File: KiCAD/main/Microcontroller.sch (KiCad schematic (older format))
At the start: 9 parts

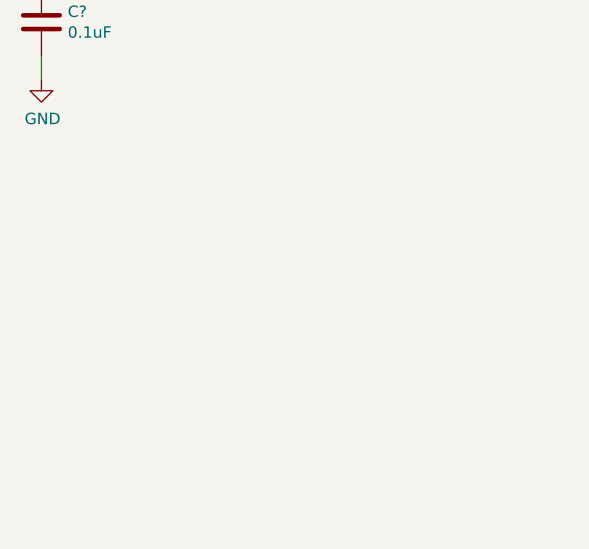
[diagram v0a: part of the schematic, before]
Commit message: Add programming header for the microcontroller
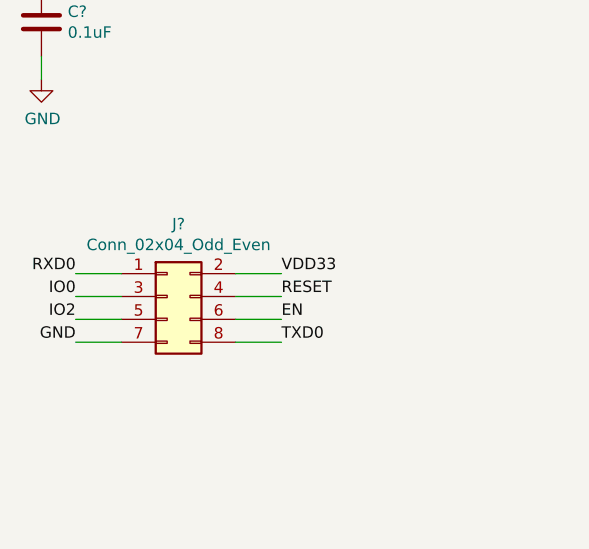
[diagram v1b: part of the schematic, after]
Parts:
- added J?: Conn_02x04_Odd_Even, symbol Connector_Generic:Conn_02x04_Odd_Even
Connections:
- net +3V3: now also J?.2 (Pin_2)
- net EN: now also J?.6 (Pin_6)
- net GND: now also J?.7 (Pin_7)
- net IO0: now also J?.3 (Pin_3)
- net IO2: now also J?.5 (Pin_5)
- net RXD0: now also J?.1 (Pin_1)
- net TXD0: now also J?.8 (Pin_8)
- new net RESET: J?.4 (Pin_4)
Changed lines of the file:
@@
 Text Label 9350 2600 0    50   ~ 0
 TXD0
+$Comp
+L Connector_Generic:Conn_02x04_Odd_Even J?
+U 1 1 5FC4BA04
+P 1650 4500
+F 0 "J?" H 1700 4817 50  0000 C CNN
+F 1 "Conn_02x04_Odd_Even" H 1700 4726 50  0000 C CNN
+F 2 "" H 1650 4500 50  0001 C CNN
+F 3 "~" H 1650 4500 50  0001 C CNN
+	1    1650 4500
+	1    0    0    -1
+$EndComp
+Text Label 1250 4500 2    50   ~ 0
+IO0
+Wire Wire Line
+	1250 4400 1450 4400
+Wire Wire Line
+	1950 4400 2150 4400
+Wire Wire Line
+	1950 4500 2150 4500
+Wire Wire Line
+	1950 4600 2150 4600
+Wire Wire Line
+	1950 4700 2150 4700
+Wire Wire Line
+	1450 4500 1250 4500
+Wire Wire Line
+	1450 4600 1250 4600
+Wire Wire Line
+	1450 4700 1250 4700
+Text Label 1250 4400 2    50   ~ 0
+RXD0
+Text Label 1250 4600 2    50   ~ 0
+IO2
+Text Label 1250 4700 2    50   ~ 0
+GND
+Text Label 2150 4400 0    50   ~ 0
+VDD33
+Text Label 2150 4500 0    50   ~ 0
+RESET
+Text Label 2150 4600 0    50   ~ 0
+EN
+Text Label 2150 4700 0    50   ~ 0
+TXD0
 $EndSCHEMATC

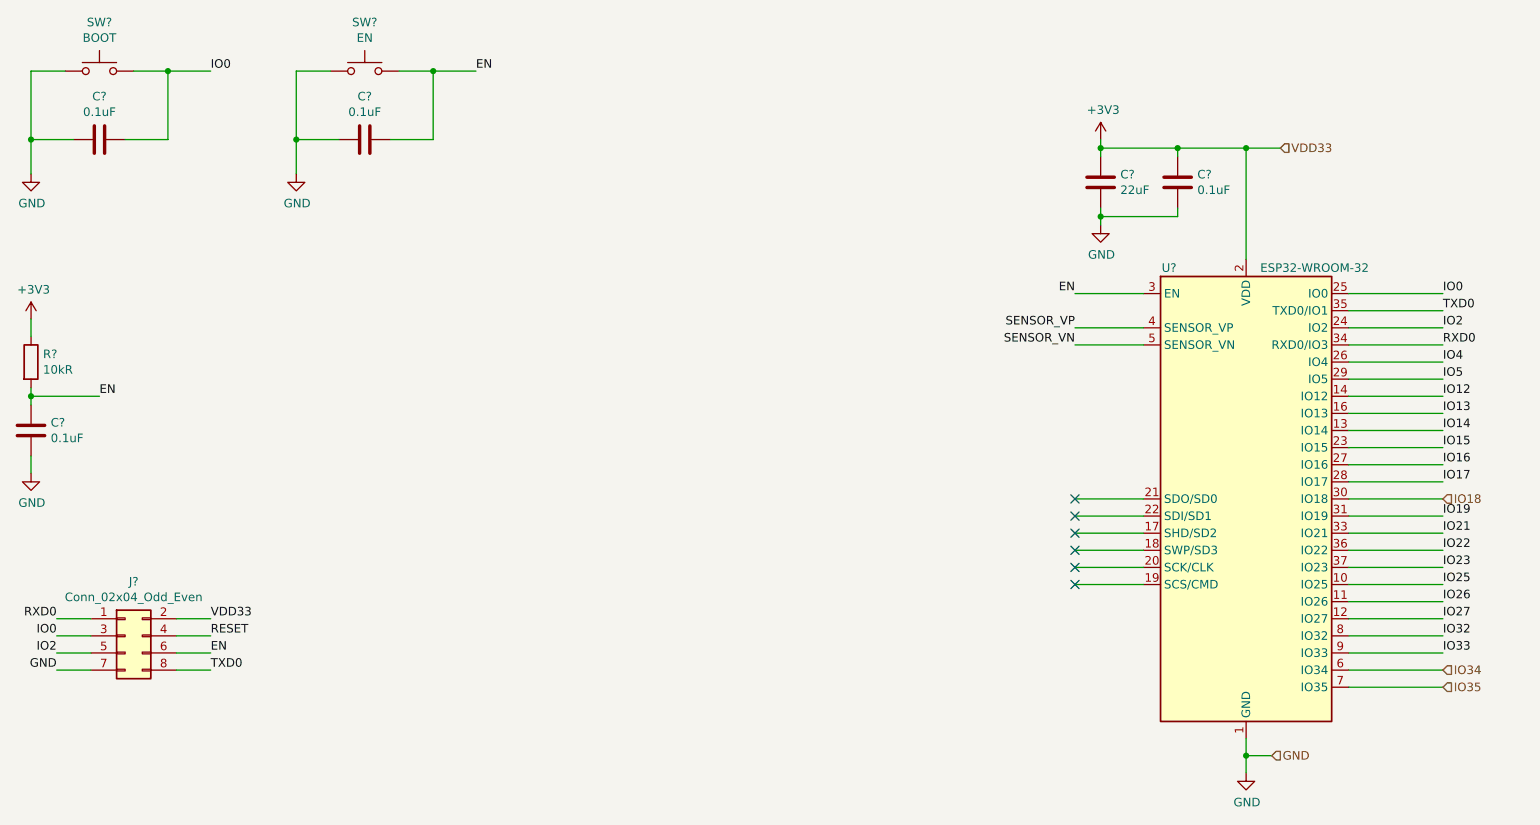
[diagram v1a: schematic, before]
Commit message: Rename EN button to RESET
and add comment about the ENABLE and RESET signals from the programming header
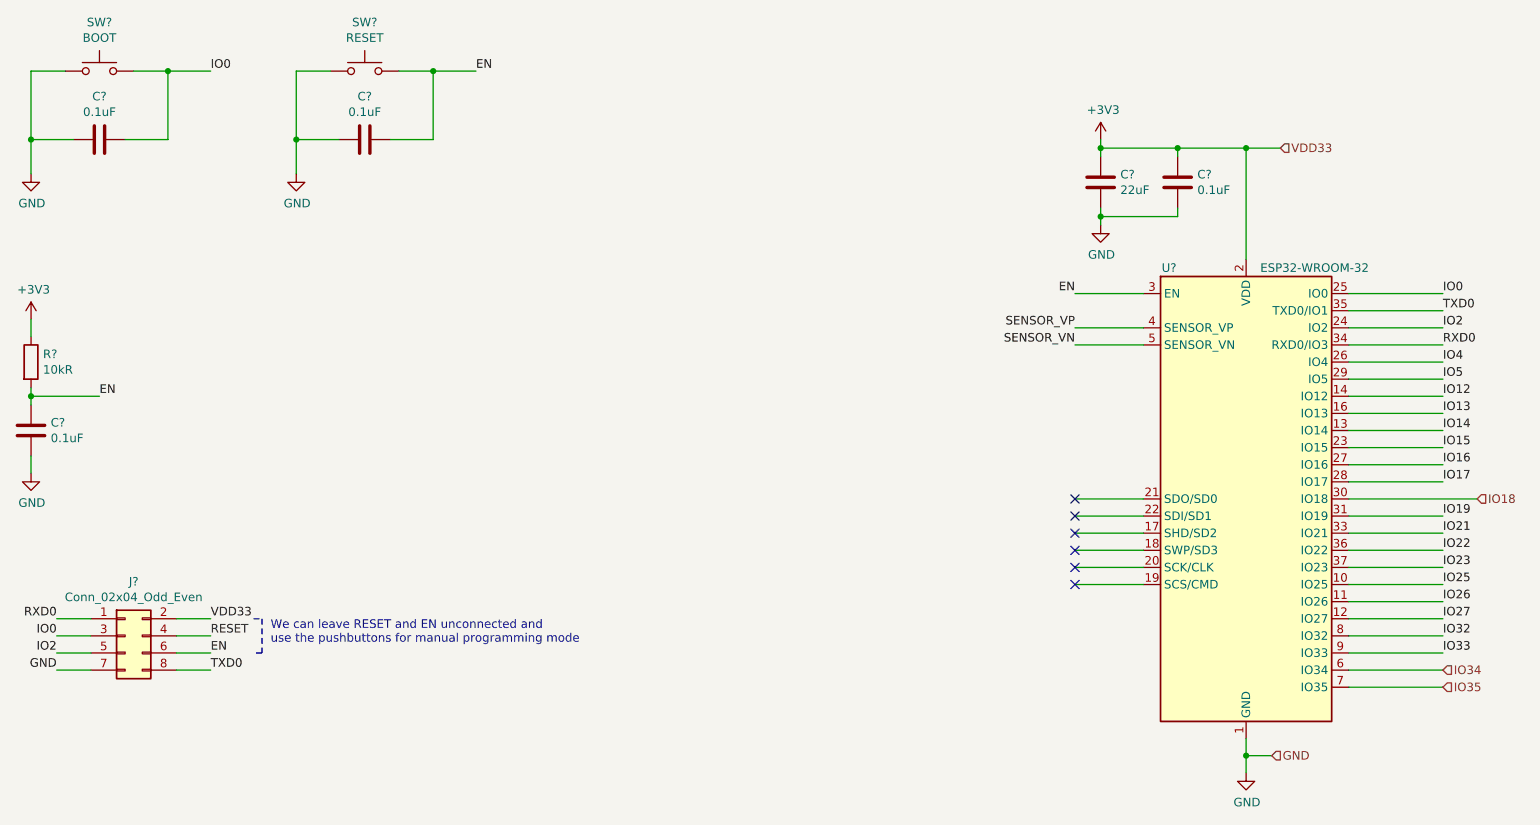
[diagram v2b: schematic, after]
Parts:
- SW?: value EN -> RESET
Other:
- note added: "We can leave RESET and EN unconnected and\nuse the pushbuttons for manual programming mode"
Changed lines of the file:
@@
 P 3050 1200
 F 0 "SW?" H 3050 1485 50  0000 C CNN
-F 1 "EN" H 3050 1394 50  0000 C CNN
+F 1 "RESET" H 3050 1394 50  0000 C CNN
 F 2 "" H 3050 1400 50  0001 C CNN
 F 3 "~" H 3050 1400 50  0001 C CNN
@@
 	8800 3600 9350 3600
 Wire Wire Line
-	8800 3700 9350 3700
-Wire Wire Line
 	8800 3800 9350 3800
 Wire Wire Line
@@
 Wire Wire Line
 	8800 4800 9350 4800
-Text HLabel 9350 3700 2    50   Input ~ 0
+Text HLabel 9550 3700 2    50   Input ~ 0
 IO18
 Text HLabel 9350 4700 2    50   Input ~ 0
@@
 Text Label 2150 4700 0    50   ~ 0
 TXD0
+Text Notes 2500 4550 0    50   ~ 0
+We can leave RESET and EN unconnected and\nuse the pushbuttons for manual programming mode
+Wire Notes Line
+	2400 4400 2450 4400
+Wire Notes Line
+	2450 4400 2450 4600
+Wire Notes Line
+	2450 4600 2400 4600
+Wire Wire Line
+	8800 3700 9550 3700
 $EndSCHEMATC

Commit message: Assign footprints to components on the microcontroller sheet
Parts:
- C? (x5): footprint (none) -> Capacitor_SMD:C_1206_3216Metric
- J?: footprint (none) -> Connector_PinHeader_2.54mm:PinHeader_2x04_P2.54mm_Vertical
- SW? (x2): footprint (none) -> Button_Switch_SMD:SW_SPST_B3S-1000
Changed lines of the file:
@@
 F 0 "C?" H 1215 3346 50  0000 L CNN
 F 1 "0.1uF" H 1215 3255 50  0000 L CNN
-F 2 "" H 1138 3150 50  0001 C CNN
+F 2 "Capacitor_SMD:C_1206_3216Metric" H 1138 3150 50  0001 C CNN
 F 3 "~" H 1100 3300 50  0001 C CNN
 F 4 "50V" H 1215 3255 50  0001 L CNN "Voltage"
@@
 F 0 "C?" H 7915 1896 50  0000 L CNN
 F 1 "0.1uF" H 7915 1805 50  0000 L CNN
-F 2 "" H 7838 1700 50  0001 C CNN
+F 2 "Capacitor_SMD:C_1206_3216Metric" H 7838 1700 50  0001 C CNN
 F 3 "~" H 7800 1850 50  0001 C CNN
 F 4 "50V" H 7915 1759 50  0001 L CNN "Voltage"
@@
 F 0 "C?" H 7465 1896 50  0000 L CNN
 F 1 "22uF" H 7465 1805 50  0000 L CNN
-F 2 "" H 7388 1700 50  0001 C CNN
+F 2 "Capacitor_SMD:C_1206_3216Metric" H 7388 1700 50  0001 C CNN
 F 3 "~" H 7350 1850 50  0001 C CNN
 F 4 "10V" H 7465 1759 50  0001 L CNN "Voltage"
@@
 F 0 "C?" V 1752 1600 50  0000 C CNN
 F 1 "0.1uF" V 1661 1600 50  0000 C CNN
-F 2 "" H 1538 1450 50  0001 C CNN
+F 2 "Capacitor_SMD:C_1206_3216Metric" H 1538 1450 50  0001 C CNN
 F 3 "~" H 1500 1600 50  0001 C CNN
 F 4 "50V" V 1500 1600 50  0001 C CNN "Voltage"
@@
 F 0 "SW?" H 1500 1485 50  0000 C CNN
 F 1 "BOOT" H 1500 1394 50  0000 C CNN
-F 2 "" H 1500 1400 50  0001 C CNN
+F 2 "Button_Switch_SMD:SW_SPST_B3S-1000" H 1500 1400 50  0001 C CNN
 F 3 "~" H 1500 1400 50  0001 C CNN
 	1    1500 1200
@@
 F 0 "C?" V 3302 1600 50  0000 C CNN
 F 1 "0.1uF" V 3211 1600 50  0000 C CNN
-F 2 "" H 3088 1450 50  0001 C CNN
+F 2 "Capacitor_SMD:C_1206_3216Metric" H 3088 1450 50  0001 C CNN
 F 3 "~" H 3050 1600 50  0001 C CNN
 F 4 "50V" V 3050 1600 50  0001 C CNN "Voltage"
@@
 F 0 "SW?" H 3050 1485 50  0000 C CNN
 F 1 "RESET" H 3050 1394 50  0000 C CNN
-F 2 "" H 3050 1400 50  0001 C CNN
+F 2 "Button_Switch_SMD:SW_SPST_B3S-1000" H 3050 1400 50  0001 C CNN
 F 3 "~" H 3050 1400 50  0001 C CNN
 	1    3050 1200
@@
 F 0 "J?" H 1700 4817 50  0000 C CNN
 F 1 "Conn_02x04_Odd_Even" H 1700 4726 50  0000 C CNN
-F 2 "" H 1650 4500 50  0001 C CNN
+F 2 "Connector_PinHeader_2.54mm:PinHeader_2x04_P2.54mm_Vertical" H 1650 4500 50  0001 C CNN
 F 3 "~" H 1650 4500 50  0001 C CNN
 	1    1650 4500

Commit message: Add simple pcb design
still buggy
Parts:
- R2: renamed from R?; footprint (none) -> Resistor_SMD:R_1206_3216Metric
- SW1, SW2: renamed from SW?; footprint Button_Switch_SMD:SW_SPST_B3S-1000 -> Button_Switch_SMD:SW_SPST_PTS645
- gave numbers to parts that had none: 7
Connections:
- net EN: no longer J5.6 (Pin_6)
- net RESET: no longer names the net of J5.4 (Pin_4)
- no-connect marks 6 -> 8
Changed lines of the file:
@@
 $Descr A4 11693 8268
 encoding utf-8
-Sheet 6 6
+Sheet 2 2
 Title "ESP32-DevKitC-V4"
 Date "2020-10-23"
@@
 $EndDescr
 $Comp
-L RF_Module:ESP32-WROOM-32 U?
+L RF_Module:ESP32-WROOM-32 U1
 U 1 1 5F93B762
 P 8200 3700
-F 0 "U?" H 7750 5050 50  0000 C CNN
+F 0 "U1" H 7750 5050 50  0000 C CNN
 F 1 "ESP32-WROOM-32" H 8600 5050 50  0000 C CNN
 F 2 "RF_Module:ESP32-WROOM-32" H 8200 2200 50  0001 C CNN
@@
 $EndComp
 $Comp
-L power:+3V3 #PWR?
+L power:+3V3 #PWR03
 U 1 1 5F9419AA
 P 1100 2650
-F 0 "#PWR?" H 1100 2500 50  0001 C CNN
+F 0 "#PWR03" H 1100 2500 50  0001 C CNN
 F 1 "+3V3" H 1115 2823 50  0000 C CNN
 F 2 "" H 1100 2650 50  0001 C CNN
@@
 $EndComp
 $Comp
-L Device:R R?
+L Device:R R2
 U 1 1 5F94208F
 P 1100 2900
-F 0 "R?" H 1170 2946 50  0000 L CNN
+F 0 "R2" H 1170 2946 50  0000 L CNN
 F 1 "10kR" H 1170 2855 50  0000 L CNN
-F 2 "" V 1030 2900 50  0001 C CNN
+F 2 "Resistor_SMD:R_1206_3216Metric" V 1030 2900 50  0001 C CNN
 F 3 "~" H 1100 2900 50  0001 C CNN
 	1    1100 2900
@@
 $EndComp
 $Comp
-L Device:C C?
+L Device:C C1
 U 1 1 5F9429EB
 P 1100 3300
-F 0 "C?" H 1215 3346 50  0000 L CNN
+F 0 "C1" H 1215 3346 50  0000 L CNN
 F 1 "0.1uF" H 1215 3255 50  0000 L CNN
 F 2 "Capacitor_SMD:C_1206_3216Metric" H 1138 3150 50  0001 C CNN
@@
 $EndComp
 $Comp
-L power:GND #PWR?
+L power:GND #PWR04
 U 1 1 5F942C61
 P 1100 3550
-F 0 "#PWR?" H 1100 3300 50  0001 C CNN
+F 0 "#PWR04" H 1100 3300 50  0001 C CNN
 F 1 "GND" H 1105 3377 50  0000 C CNN
 F 2 "" H 1100 3550 50  0001 C CNN
@@
 	1100 2750 1100 2650
 $Comp
-L power:+3V3 #PWR?
+L power:+3V3 #PWR06
 U 1 1 5F943FB0
 P 7350 1600
-F 0 "#PWR?" H 7350 1450 50  0001 C CNN
+F 0 "#PWR06" H 7350 1450 50  0001 C CNN
 F 1 "+3V3" H 7365 1773 50  0000 C CNN
 F 2 "" H 7350 1600 50  0001 C CNN
@@
 $EndComp
 $Comp
-L Device:C C?
+L Device:C C5
 U 1 1 5F9451F0
 P 7800 1850
-F 0 "C?" H 7915 1896 50  0000 L CNN
+F 0 "C5" H 7915 1896 50  0000 L CNN
 F 1 "0.1uF" H 7915 1805 50  0000 L CNN
 F 2 "Capacitor_SMD:C_1206_3216Metric" H 7838 1700 50  0001 C CNN
@@
 $EndComp
 $Comp
-L Device:C C?
+L Device:C C4
 U 1 1 5F946123
 P 7350 1850
-F 0 "C?" H 7465 1896 50  0000 L CNN
+F 0 "C4" H 7465 1896 50  0000 L CNN
 F 1 "22uF" H 7465 1805 50  0000 L CNN
 F 2 "Capacitor_SMD:C_1206_3216Metric" H 7388 1700 50  0001 C CNN
@@
 	7350 2050 7350 2000
 $Comp
-L power:GND #PWR?
+L power:GND #PWR07
 U 1 1 5F947B11
 P 7350 2100
-F 0 "#PWR?" H 7350 1850 50  0001 C CNN
+F 0 "#PWR07" H 7350 1850 50  0001 C CNN
 F 1 "GND" H 7355 1927 50  0000 C CNN
 F 2 "" H 7350 2100 50  0001 C CNN
@@
 	8200 2300 8200 1650
 $Comp
-L power:GND #PWR?
+L power:GND #PWR08
 U 1 1 5F95286C
 P 8200 5300
-F 0 "#PWR?" H 8200 5050 50  0001 C CNN
+F 0 "#PWR08" H 8200 5050 50  0001 C CNN
 F 1 "GND" H 8205 5127 50  0000 C CNN
 F 2 "" H 8200 5300 50  0001 C CNN
@@
 	8800 2800 9350 2800
 $Comp
-L power:GND #PWR?
+L power:GND #PWR02
 U 1 1 5F958154
 P 1100 1800
-F 0 "#PWR?" H 1100 1550 50  0001 C CNN
+F 0 "#PWR02" H 1100 1550 50  0001 C CNN
 F 1 "GND" H 1105 1627 50  0000 C CNN
 F 2 "" H 1100 1800 50  0001 C CNN
@@
 $EndComp
 $Comp
-L Device:C C?
+L Device:C C2
 U 1 1 5F9586F2
 P 1500 1600
-F 0 "C?" V 1752 1600 50  0000 C CNN
+F 0 "C2" V 1752 1600 50  0000 C CNN
 F 1 "0.1uF" V 1661 1600 50  0000 C CNN
 F 2 "Capacitor_SMD:C_1206_3216Metric" H 1538 1450 50  0001 C CNN
@@
 	1100 1600 1100 1800
 $Comp
-L Switch:SW_Push SW?
+L Switch:SW_Push SW1
 U 1 1 5F9596F6
 P 1500 1200
-F 0 "SW?" H 1500 1485 50  0000 C CNN
+F 0 "SW1" H 1500 1485 50  0000 C CNN
 F 1 "BOOT" H 1500 1394 50  0000 C CNN
-F 2 "Button_Switch_SMD:SW_SPST_B3S-1000" H 1500 1400 50  0001 C CNN
+F 2 "Button_Switch_SMD:SW_SPST_PTS645" H 1500 1400 50  0001 C CNN
 F 3 "~" H 1500 1400 50  0001 C CNN
 	1    1500 1200
@@
 Connection ~ 1900 1200
 $Comp
-L power:GND #PWR?
+L power:GND #PWR05
 U 1 1 5F960D2F
 P 2650 1800
-F 0 "#PWR?" H 2650 1550 50  0001 C CNN
+F 0 "#PWR05" H 2650 1550 50  0001 C CNN
 F 1 "GND" H 2655 1627 50  0000 C CNN
 F 2 "" H 2650 1800 50  0001 C CNN
@@
 $EndComp
 $Comp
-L Device:C C?
+L Device:C C3
 U 1 1 5F960D36
 P 3050 1600
-F 0 "C?" V 3302 1600 50  0000 C CNN
+F 0 "C3" V 3302 1600 50  0000 C CNN
 F 1 "0.1uF" V 3211 1600 50  0000 C CNN
 F 2 "Capacitor_SMD:C_1206_3216Metric" H 3088 1450 50  0001 C CNN
@@
 	2650 1600 2650 1800
 $Comp
-L Switch:SW_Push SW?
+L Switch:SW_Push SW2
 U 1 1 5F960D3E
 P 3050 1200
-F 0 "SW?" H 3050 1485 50  0000 C CNN
+F 0 "SW2" H 3050 1485 50  0000 C CNN
 F 1 "RESET" H 3050 1394 50  0000 C CNN
-F 2 "Button_Switch_SMD:SW_SPST_B3S-1000" H 3050 1400 50  0001 C CNN
+F 2 "Button_Switch_SMD:SW_SPST_PTS645" H 3050 1400 50  0001 C CNN
 F 3 "~" H 3050 1400 50  0001 C CNN
 	1    3050 1200
@@
 TXD0
 $Comp
-L Connector_Generic:Conn_02x04_Odd_Even J?
+L Connector_Generic:Conn_02x04_Odd_Even J5
 U 1 1 5FC4BA04
 P 1650 4500
-F 0 "J?" H 1700 4817 50  0000 C CNN
+F 0 "J5" H 1700 4817 50  0000 C CNN
 F 1 "Conn_02x04_Odd_Even" H 1700 4726 50  0000 C CNN
 F 2 "Connector_PinHeader_2.54mm:PinHeader_2x04_P2.54mm_Vertical" H 1650 4500 50  0001 C CNN
@@
 Text Label 2150 4400 0    50   ~ 0
 VDD33
-Text Label 2150 4500 0    50   ~ 0
-RESET
-Text Label 2150 4600 0    50   ~ 0
-EN
 Text Label 2150 4700 0    50   ~ 0
 TXD0
@@
 Wire Wire Line
 	8800 3700 9550 3700
+NoConn ~ 2150 4500
+NoConn ~ 2150 4600
 $EndSCHEMATC

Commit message: alimentação e proteção
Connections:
- net IO15 renamed I015
- net IO21 renamed I021
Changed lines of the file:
@@
 Wire Wire Line
 	8800 4800 9350 4800
-Text HLabel 9550 3700 2    50   Input ~ 0
+Text HLabel 9350 3700 2    50   Input ~ 0
 IO18
 Text HLabel 9350 4700 2    50   Input ~ 0
@@
 Text Label 7200 2500 2    50   ~ 0
 EN
-Text Label 9350 4600 0    50   ~ 0
-IO33
-Text Label 9350 4500 0    50   ~ 0
-IO32
-Text Label 9350 4400 0    50   ~ 0
-IO27
-Text Label 9350 4300 0    50   ~ 0
-IO26
-Text Label 9350 4200 0    50   ~ 0
-IO25
-Text Label 9350 3800 0    50   ~ 0
-IO19
-Text Label 9350 3600 0    50   ~ 0
-IO17
-Text Label 9350 3500 0    50   ~ 0
-IO16
-Text Label 9350 3400 0    50   ~ 0
-IO15
-Text Label 9350 3300 0    50   ~ 0
-IO14
-Text Label 9350 3200 0    50   ~ 0
-IO13
 Text Label 9350 3100 0    50   ~ 0
 IO12
@@
 Text Label 9350 2500 0    50   ~ 0
 IO0
-Text Label 9350 3900 0    50   ~ 0
-IO21
-Text Label 9350 4000 0    50   ~ 0
-IO22
-Text Label 9350 4100 0    50   ~ 0
-IO23
 Text Label 7200 2700 2    50   ~ 0
 SENSOR_VP
@@
 Wire Notes Line
 	2450 4600 2400 4600
-Wire Wire Line
-	8800 3700 9550 3700
 NoConn ~ 2150 4500
 NoConn ~ 2150 4600
+Text HLabel 9350 3800 2    50   Input ~ 0
+IO19
+Text HLabel 9350 3900 2    50   Input ~ 0
+I021
+Text HLabel 9350 4000 2    50   Input ~ 0
+IO22
+Text HLabel 9350 4600 2    50   Input ~ 0
+IO33
+Text HLabel 9350 4100 2    50   Input ~ 0
+IO23
+Text HLabel 9350 4200 2    50   Input ~ 0
+IO25
+Text HLabel 9350 4300 2    50   Input ~ 0
+IO26
+Text HLabel 9350 4400 2    50   Input ~ 0
+IO27
+Text HLabel 9350 4500 2    50   Input ~ 0
+IO32
+Wire Wire Line
+	8800 3700 9350 3700
+Text HLabel 9350 3600 2    50   Input ~ 0
+IO17
+Text HLabel 9350 3500 2    50   Input ~ 0
+IO16
+Text HLabel 9350 3400 2    50   Input ~ 0
+I015
+Text HLabel 9350 3300 2    50   Input ~ 0
+IO14
+Text Label 9350 3200 0    50   ~ 0
+IO13
 $EndSCHEMATC

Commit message: algumas correções
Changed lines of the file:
@@
 Text HLabel 9350 3300 2    50   Input ~ 0
 IO14
-Text Label 9350 3200 0    50   ~ 0
+Text HLabel 9350 3200 2    50   Input ~ 0
 IO13
 $EndSCHEMATC
